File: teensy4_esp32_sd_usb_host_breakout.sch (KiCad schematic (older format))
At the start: 36 parts, among them J1 Conn_01x14, J2 USB_A, J3 Conn_01x14, J4 Micro_SD_Card_Det_Hirose_DM3AT, J5 Conn_01x08, J6 Conn_01x04, J7 Conn_01x01, SW2 PROGRAM, U1 TPD3S014, U2 TLV75733PDBVR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

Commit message: More details
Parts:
- JP1: footprint Jumper:SolderJumper-2_P1.3mm_Bridged_RoundedPad1.0x1.5mm -> Jumper:SolderJumper-2_P1.3mm_Open_RoundedPad1.0x1.5mm; symbol Jumper:SolderJumper_2_Bridged -> Jumper:SolderJumper_2_Open
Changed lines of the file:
@@
 $EndComp
 $Comp
-L Jumper:SolderJumper_2_Bridged JP1
+L Jumper:SolderJumper_2_Open JP1
 U 1 1 5D8BA9A0
 P 7950 2400
 F 0 "JP1" H 7950 2605 50  0000 C CNN
 F 1 "Teensy 3.3" H 7950 2514 50  0000 C CNN
-F 2 "Jumper:SolderJumper-2_P1.3mm_Bridged_RoundedPad1.0x1.5mm" H 7950 2400 50  0001 C CNN
+F 2 "Jumper:SolderJumper-2_P1.3mm_Open_RoundedPad1.0x1.5mm" H 7950 2400 50  0001 C CNN
 F 3 "~" H 7950 2400 50  0001 C CNN
 	1    7950 2400
@@
 U 1 1 5E785260
 P 4550 2500
-F 0 "J6" H 4550 2300 50  0000 C CNN
-F 1 "Conn_01x04" H 4350 2200 50  0000 C CNN
+F 0 "J6" H 4550 2200 50  0000 C CNN
+F 1 "Conn_01x04" H 4350 2100 50  0000 C CNN
 F 2 "Connector_PinHeader_2.54mm:PinHeader_1x04_P2.54mm_Vertical" H 4550 2500 50  0001 C CNN
 F 3 "~" H 4550 2500 50  0001 C CNN

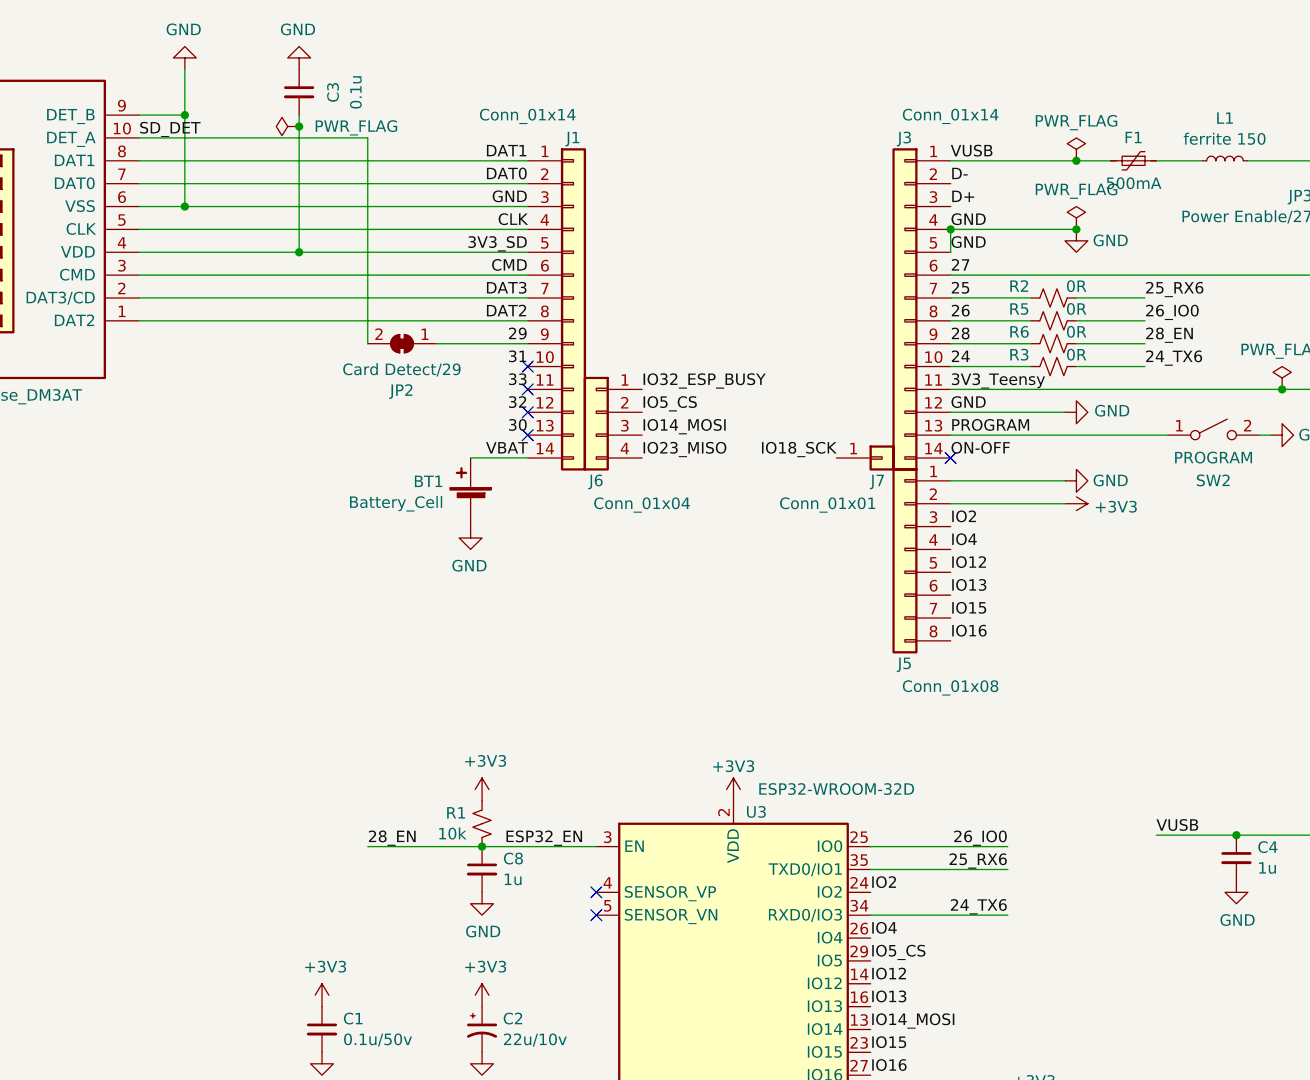
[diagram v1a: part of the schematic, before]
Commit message: Update readme, fix via sizes
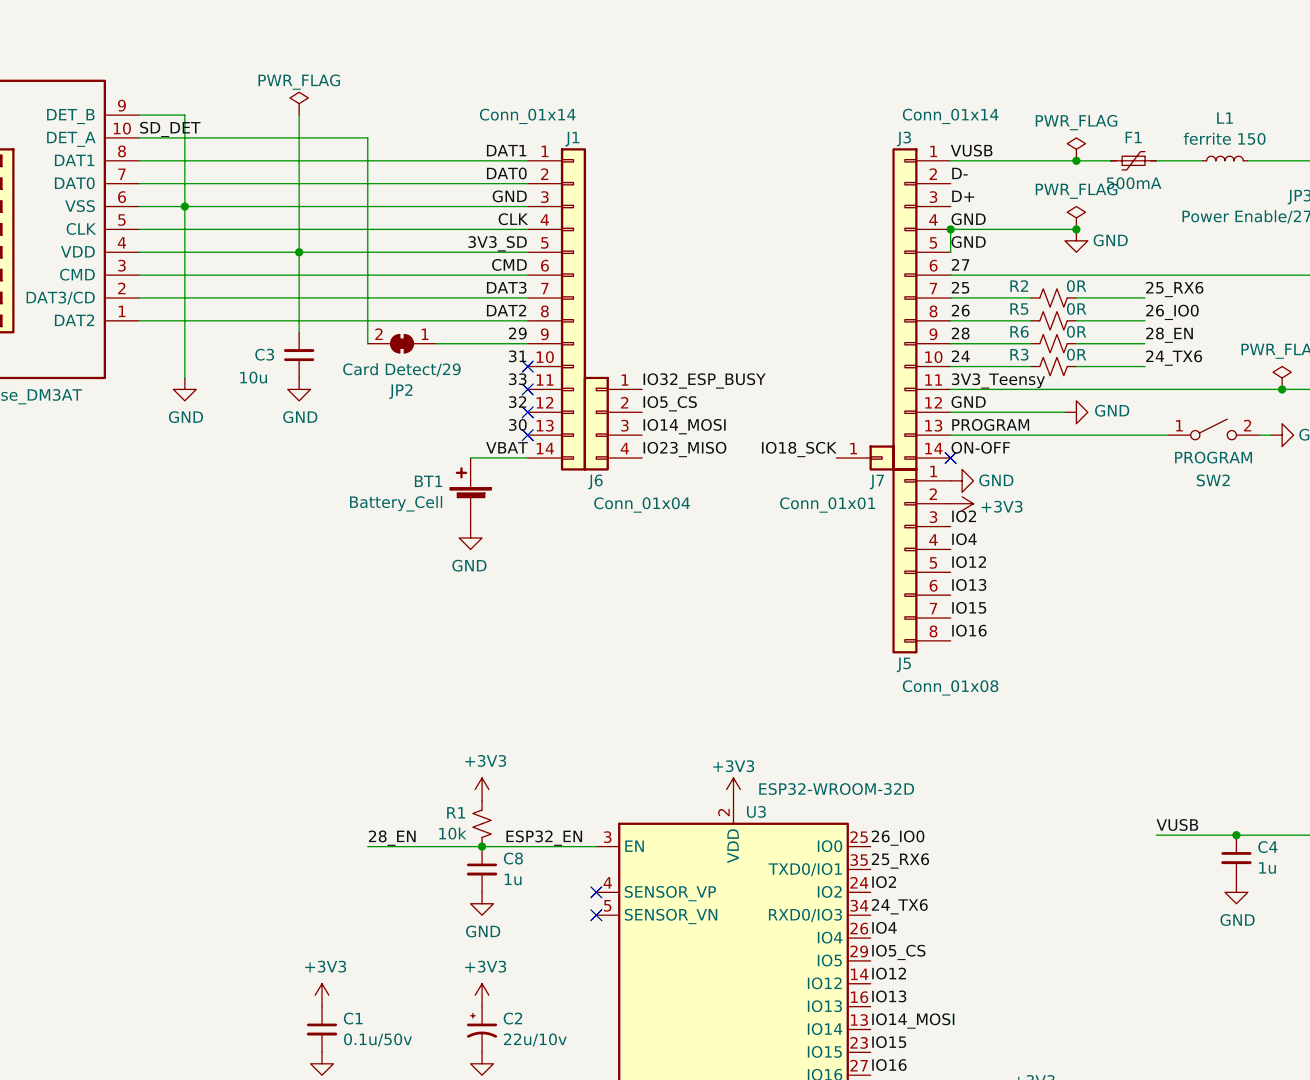
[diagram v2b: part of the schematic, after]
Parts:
- C3: value 0.1u -> 10u
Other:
- moved on the sheet: C3
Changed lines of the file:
@@
 L power:GND #PWR0109
 U 1 1 5DE46B96
-P 2750 1000
-F 0 "#PWR0109" H 2750 750 50  0001 C CNN
-F 1 "GND" H 2755 827 50  0000 C CNN
-F 2 "" H 2750 1000 50  0001 C CNN
-F 3 "" H 2750 1000 50  0001 C CNN
-	1    2750 1000
-	-1   0    0    1
+P 2750 2350
+F 0 "#PWR0109" H 2750 2100 50  0001 C CNN
+F 1 "GND" H 2755 2177 50  0000 C CNN
+F 2 "" H 2750 2350 50  0001 C CNN
+F 3 "" H 2750 2350 50  0001 C CNN
+	1    2750 2350
+	1    0    0    -1
 $EndComp
 Wire Wire Line
@@
 L Device:C_Small C3
 U 1 1 5DE0B848
-P 3250 1100
-F 0 "C3" V 3400 1100 50  0000 C CNN
-F 1 "0.1u" V 3500 1100 50  0000 C CNN
-F 2 "Capacitor_SMD:C_0805_2012Metric_Pad1.15x1.40mm_HandSolder" H 3250 1100 50  0001 C CNN
-F 3 "~" H 3250 1100 50  0001 C CNN
-	1    3250 1100
-	1    0    0    -1
+P 3250 2250
+F 0 "C3" H 3400 2250 50  0000 C CNN
+F 1 "10u" H 3450 2350 50  0000 C CNN
+F 2 "Capacitor_SMD:C_0805_2012Metric_Pad1.15x1.40mm_HandSolder" H 3250 2250 50  0001 C CNN
+F 3 "~" H 3250 2250 50  0001 C CNN
+	1    3250 2250
+	-1   0    0    1
 $EndComp
 Wire Wire Line
@@
 Wire Wire Line
 	9750 1700 10050 1700
-Wire Wire Line
-	3250 1200 3250 1250
 Connection ~ 3250 1800
 Wire Wire Line
@@
 Wire Wire Line
 	3550 1300 2550 1300
-Wire Wire Line
-	2750 1200 2750 1000
-Connection ~ 2750 1200
 $Comp
 L power:GND #PWR0101
 U 1 1 5DE50660
-P 3250 1000
-F 0 "#PWR0101" H 3250 750 50  0001 C CNN
-F 1 "GND" H 3255 827 50  0000 C CNN
-F 2 "" H 3250 1000 50  0001 C CNN
-F 3 "" H 3250 1000 50  0001 C CNN
-	1    3250 1000
-	-1   0    0    1
+P 3250 2350
+F 0 "#PWR0101" H 3250 2100 50  0001 C CNN
+F 1 "GND" H 3255 2177 50  0000 C CNN
+F 2 "" H 3250 2350 50  0001 C CNN
+F 3 "" H 3250 2350 50  0001 C CNN
+	1    3250 2350
+	1    0    0    -1
 $EndComp
 $Comp
@@
 	0    1    1    0
 $EndComp
-Text Label 6350 4700 2    50   ~ 0
+Text Label 5750 4700 0    50   ~ 0
 24_TX6
-Text Label 6350 4500 2    50   ~ 0
+Text Label 5750 4500 0    50   ~ 0
 25_RX6
-Wire Wire Line
-	5750 4400 6350 4400
-Text Label 6350 4400 2    50   ~ 0
+Text Label 5750 4400 0    50   ~ 0
 26_IO0
 Text Label 4150 4400 0    50   ~ 0
@@
 L power:GND #PWR0112
 U 1 1 5E78E159
-P 6600 2800
-F 0 "#PWR0112" H 6600 2550 50  0001 C CNN
-F 1 "GND" V 6600 2600 50  0000 C CNN
-F 2 "" H 6600 2800 50  0001 C CNN
-F 3 "" H 6600 2800 50  0001 C CNN
-	1    6600 2800
+P 6100 2800
+F 0 "#PWR0112" H 6100 2550 50  0001 C CNN
+F 1 "GND" V 6100 2600 50  0000 C CNN
+F 2 "" H 6100 2800 50  0001 C CNN
+F 3 "" H 6100 2800 50  0001 C CNN
+	1    6100 2800
 	0    -1   -1   0
 $EndComp
-Wire Wire Line
-	6100 2800 6600 2800
 Wire Wire Line
 	7350 4350 7700 4350
@@
 $EndComp
 Wire Wire Line
-	5750 4500 6350 4500
-Wire Wire Line
-	5750 4700 6350 4700
-Wire Wire Line
 	6100 2500 6600 2500
 Connection ~ 7550 2400
@@
 L power:+3V3 #PWR0107
 U 1 1 5E7A53B4
-P 6600 2900
-F 0 "#PWR0107" H 6600 2750 50  0001 C CNN
-F 1 "+3V3" V 6615 3028 50  0000 L CNN
-F 2 "" H 6600 2900 50  0001 C CNN
-F 3 "" H 6600 2900 50  0001 C CNN
-	1    6600 2900
+P 6100 2900
+F 0 "#PWR0107" H 6100 2750 50  0001 C CNN
+F 1 "+3V3" V 6115 3028 50  0000 L CNN
+F 2 "" H 6100 2900 50  0001 C CNN
+F 3 "" H 6100 2900 50  0001 C CNN
+	1    6100 2900
 	0    1    1    0
 $EndComp
-Wire Wire Line
-	6100 2900 6600 2900
 Text Label 5750 6300 0    50   ~ 0
 IO27_BLUE
@@
 L power:PWR_FLAG #FLG0104
 U 1 1 5E8E1C80
-P 3250 1250
-F 0 "#FLG0104" H 3250 1325 50  0001 C CNN
-F 1 "PWR_FLAG" V 3250 1000 50  0000 C CNN
-F 2 "" H 3250 1250 50  0001 C CNN
-F 3 "~" H 3250 1250 50  0001 C CNN
-	1    3250 1250
-	0    -1   -1   0
-$EndComp
-Connection ~ 3250 1250
-Wire Wire Line
-	3250 1250 3250 1800
+P 3250 1200
+F 0 "#FLG0104" H 3250 1275 50  0001 C CNN
+F 1 "PWR_FLAG" H 3250 1350 50  0000 C CNN
+F 2 "" H 3250 1200 50  0001 C CNN
+F 3 "~" H 3250 1200 50  0001 C CNN
+	1    3250 1200
+	1    0    0    -1
+$EndComp
 NoConn ~ 4250 2300
 NoConn ~ 4250 2400
 NoConn ~ 4250 2500
 NoConn ~ 4250 2600
+Wire Wire Line
+	3250 1200 3250 1800
+Wire Wire Line
+	2750 1600 2750 2350
+Wire Wire Line
+	3250 1800 3250 2150
 $EndSCHEMATC

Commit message: Version 1.0 Ordered
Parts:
- BT1: Digikey (none) -> BC501SM-TRCT-ND‎
- D1: Digikey (none) -> 1516-1085-1-ND
- D2: Digikey (none) -> 516-4385-1-ND‎
- J4: Digikey (none) -> HR1941CT-ND‎
- SW2: Digikey (none) -> CKN12216-1-ND‎
- U2: Digikey (none) -> 296-50414-1-ND
- U3: Digikey (none) -> 1904-1025-1-ND
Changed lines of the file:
@@
 F 2 "Connector_Card:microSD_HC_Hirose_DM3D-SF" H 3700 2400 50  0001 C CNN
 F 3 "https://www.hirose.com/product/en/download_file/key_name/DM3/category/Catalog/doc_file_id/49662/?file_category_id=4&item_id=195&is_series=1" H 1650 1800 50  0001 C CNN
+F 4 "HR1941CT-ND‎" H 1650 1700 50  0001 C CNN "Digikey"
 	1    1650 1700
 	-1   0    0    1
@@
 F 2 "RF_Module:ESP32-WROOM-32" H 5150 4100 50  0001 C CNN
 F 3 "https://www.espressif.com/sites/default/files/documentation/esp32-wroom-32d_esp32-wroom-32u_datasheet_en.pdf" H 4850 5650 50  0001 C CNN
+F 4 "1904-1025-1-ND" H 5150 5600 50  0001 C CNN "Digikey"
 	1    5150 5600
 	1    0    0    -1
@@
 F 2 "Package_TO_SOT_SMD:SOT-23-5" H 8000 4750 50  0001 C CIN
 F 3 "http://www.ti.com/lit/ds/symlink/tlv755p.pdf" H 8000 4450 50  0001 C CNN
+F 4 "296-50414-1-ND" H 8000 4450 50  0001 C CNN "Digikey"
 	1    8000 4450
 	1    0    0    -1
@@
 F 2 "BatteryHolder_MPD_BC501SM:BatteryHolder_MPD_BC501SM" V 4000 2960 50  0001 C CNN
 F 3 "~" V 4000 2960 50  0001 C CNN
+F 4 "BC501SM-TRCT-ND‎" H 4000 2900 50  0001 C CNN "Digikey"
 	1    4000 2900
 	-1   0    0    -1
@@
 F 2 "Button_Switch_SMD:SW_SPST_PTS810" H 7250 2600 50  0001 C CNN
 F 3 "~" H 7250 2600 50  0001 C CNN
+F 4 "CKN12216-1-ND‎" H 7250 2600 50  0001 C CNN "Digikey"
 	1    7250 2600
 	1    0    0    -1
@@
 F 2 "LED_SMD:LED_0805_2012Metric_Pad1.15x1.40mm_HandSolder" H 6450 5750 50  0001 C CNN
 F 3 "~" H 6450 5750 50  0001 C CNN
+F 4 "1516-1085-1-ND" H 6450 5750 50  0001 C CNN "Digikey"
 	1    6450 5750
 	0    -1   -1   0
@@
 F 2 "LED_SMD:LED_Avago_PLCC6_3x2.8mm" H 8750 5400 50  0001 C CNN
 F 3 "~" H 8750 5400 50  0001 C CNN
+F 4 "516-4385-1-ND‎" H 8750 5450 50  0001 C CNN "Digikey"
 	1    8750 5450
 	1    0    0    -1
